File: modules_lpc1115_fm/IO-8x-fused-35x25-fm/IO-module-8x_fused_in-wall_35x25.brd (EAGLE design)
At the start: 35 x 25 mm, 86 parts, among them IC1 LPC1115, IC2 ATAES132A-SHEQ-T, Q2 ASFL, U1 EEPROM, X3 MICROMATCH-10

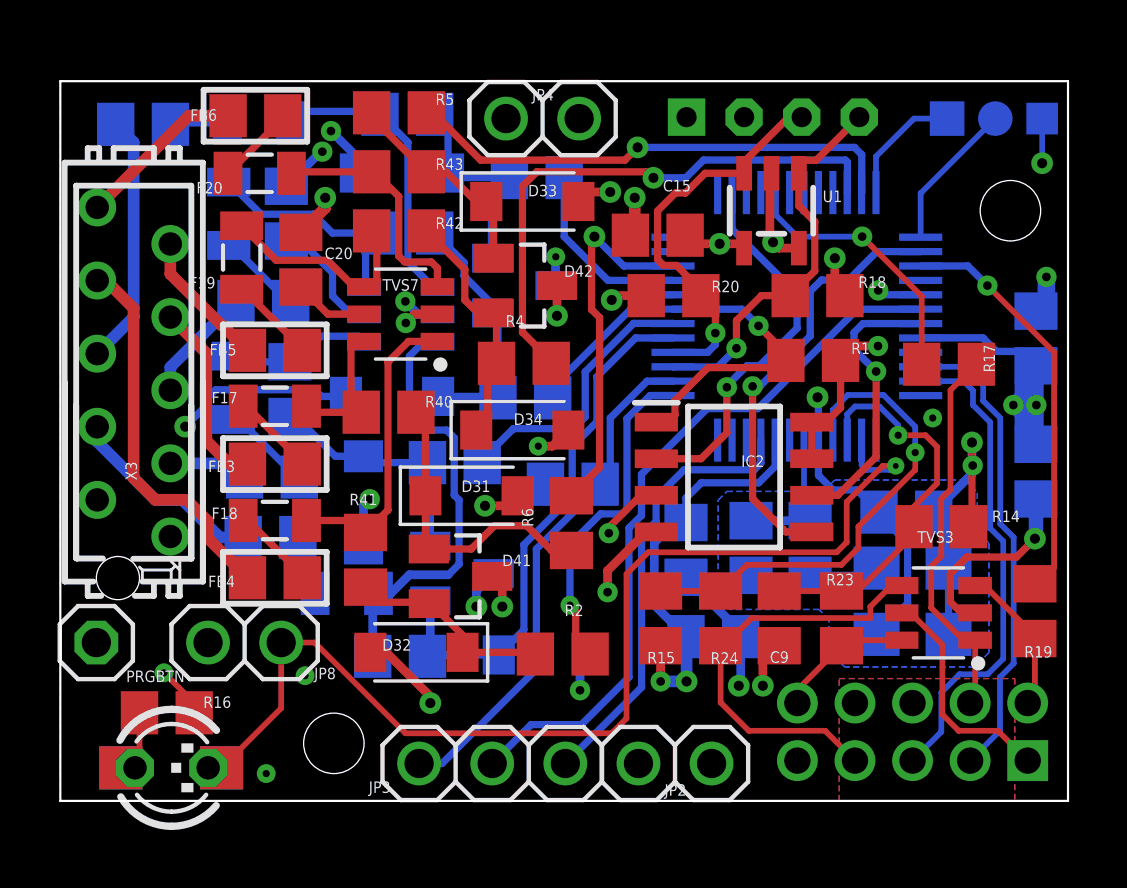
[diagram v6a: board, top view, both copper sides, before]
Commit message: [IOmodule8xUP] added missing blocking capacitor to IC2
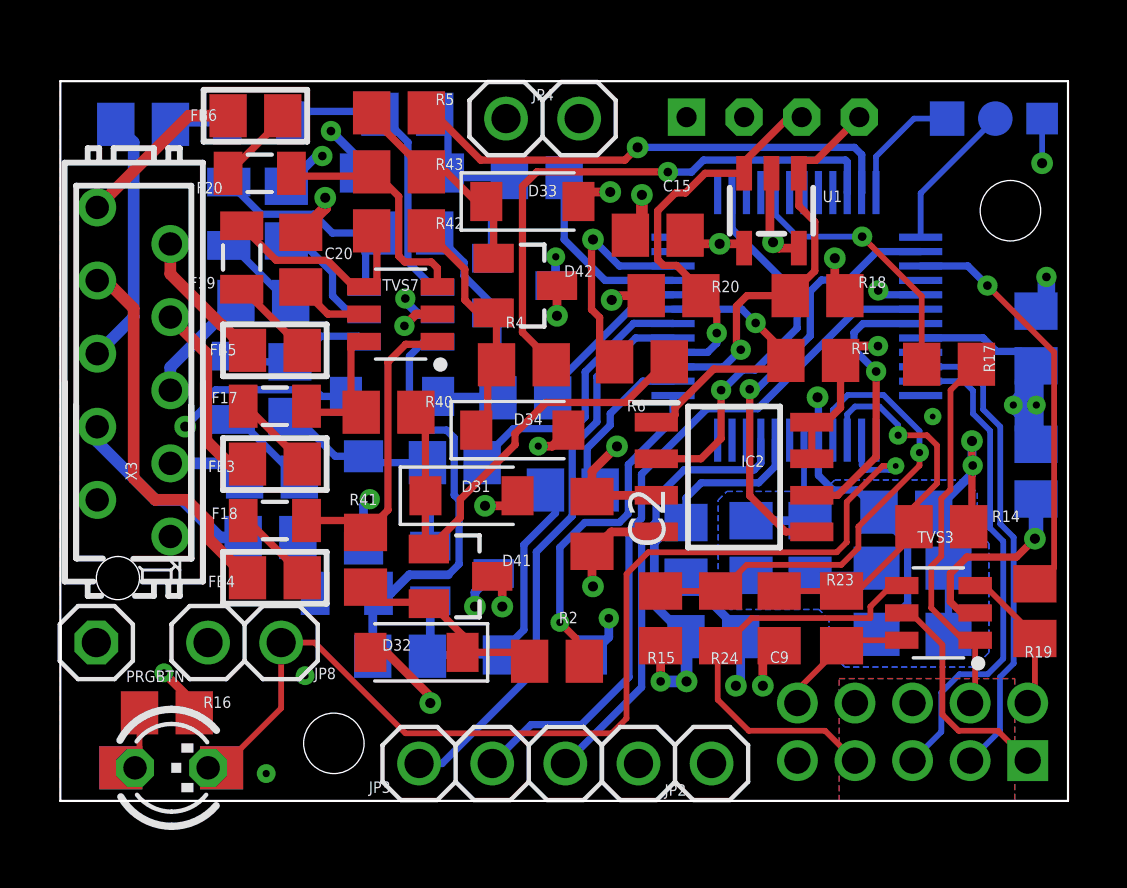
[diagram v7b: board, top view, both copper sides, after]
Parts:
- added C2: 100n, rcl:C0805
- moved R6 6.11 mm to (20.2, 15.2), turned to 180 degrees
- moved R2 0.32 mm to (17.2, 4.85)
- moved R3 0.20 mm to (17.8, 10.8)
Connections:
- net +3V3: now also C2.1
- net GND: now also C2.2
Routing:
- net IO5R: track 10.6 -> 16.6 mm
- net IO5: track 12.7 -> 7.76 mm
- net +3V3: track 63.1 -> 65.3 mm
- net GND: track 59.7 -> 61.0 mm
- net IO2: track 5.16 -> 5.82 mm
- net SCL: track 13.5 -> 14.1 mm
